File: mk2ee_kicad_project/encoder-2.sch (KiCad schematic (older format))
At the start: 7 parts, among them J11 Conn_02x6_Male, J12 Conn_01x06_Male, J13 Conn_01x06_Male, U10 AS5047D-ATSM, U11 74HC595

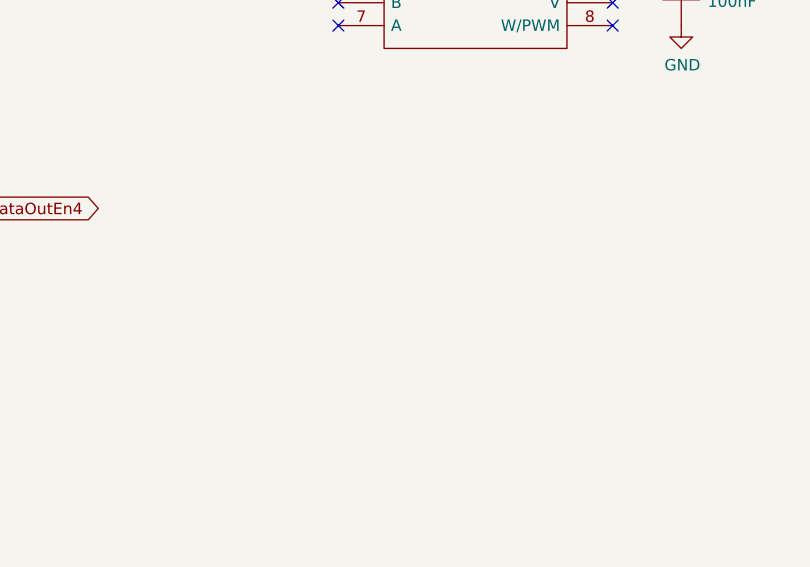
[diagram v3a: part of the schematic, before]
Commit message: New 3D model of Base part and PCB design is fixed
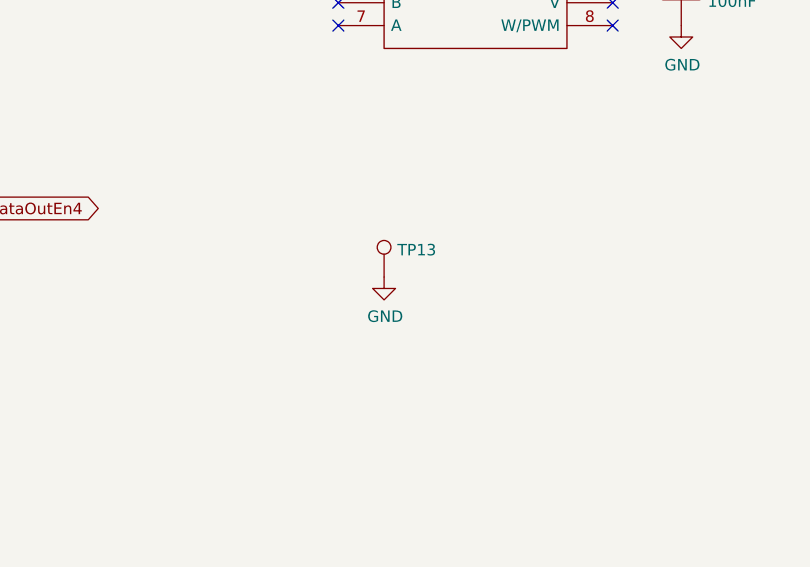
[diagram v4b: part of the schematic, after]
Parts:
- added TP13: TestPoint, TestPoint:TestPoint_THTPad_D1.0mm_Drill0.5mm, symbol Connector:TestPoint
- C22, C23: footprint Capacitor_SMD:C_1206_3216Metric -> Capacitor_SMD:C_1206_3216Metric_Pad1.42x1.75mm_HandSolder
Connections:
- net GND: now also TP13.1
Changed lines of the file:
@@
 F 0 "C23" H 7465 2596 50  0000 L CNN
 F 1 "100nF" H 7465 2505 50  0000 L CNN
-F 2 "Capacitor_SMD:C_1206_3216Metric" H 7388 2400 50  0001 C CNN
+F 2 "Capacitor_SMD:C_1206_3216Metric_Pad1.42x1.75mm_HandSolder" H 7388 2400 50  0001 C CNN
 F 3 "~" H 7350 2550 50  0001 C CNN
 F 4 "C1206C104K5RACTU" H 7350 2550 50  0001 C CNN "Name"
@@
 F 0 "C22" H 2715 2196 50  0000 L CNN
 F 1 "100nF" H 2715 2105 50  0000 L CNN
-F 2 "Capacitor_SMD:C_1206_3216Metric" H 2638 2000 50  0001 C CNN
+F 2 "Capacitor_SMD:C_1206_3216Metric_Pad1.42x1.75mm_HandSolder" H 2638 2000 50  0001 C CNN
 F 3 "~" H 2600 2150 50  0001 C CNN
 F 4 "C1206C104K5RACTU" H 2600 2150 50  0001 C CNN "Name"
@@
 	9650 2950 9900 2950
 NoConn ~ 9900 4050
+$Comp
+L Connector:TestPoint TP?
+U 1 1 608DDC15
+P 6050 3800
+AR Path="/5F455032/608DDC15" Ref="TP?"  Part="1"
+AR Path="/5F4C637B/608DDC15" Ref="TP?"  Part="1"
+AR Path="/5F475AB3/608DDC15" Ref="TP?"  Part="1"
+AR Path="/5F505E68/608DDC15" Ref="TP13"  Part="1"
+F 0 "TP13" H 6108 3918 50  0000 L CNN
+F 1 "TestPoint" H 6108 3827 50  0001 L CNN
+F 2 "TestPoint:TestPoint_THTPad_D1.0mm_Drill0.5mm" H 6250 3800 50  0001 C CNN
+F 3 "~" H 6250 3800 50  0001 C CNN
+	1    6050 3800
+	1    0    0    -1
+$EndComp
+$Comp
+L power:GND #PWR?
+U 1 1 608DF432
+P 6050 3800
+AR Path="/5F4C6CE4/608DF432" Ref="#PWR?"  Part="1"
+AR Path="/5F4C6BF4/608DF432" Ref="#PWR?"  Part="1"
+AR Path="/5F505E68/608DF432" Ref="#PWR?"  Part="1"
+F 0 "#PWR?" H 6050 3550 50  0001 C CNN
+F 1 "GND" H 6055 3627 50  0000 C CNN
+F 2 "" H 6050 3800 50  0001 C CNN
+F 3 "" H 6050 3800 50  0001 C CNN
+	1    6050 3800
+	1    0    0    -1
+$EndComp
 $EndSCHEMATC
